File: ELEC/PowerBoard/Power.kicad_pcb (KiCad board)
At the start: 2 copper layers, 42.7 x 46.7 mm, 2 parts, among them J1 CONN_01X08, J2 CONN_01X08

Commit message: Added roadmap, worked on power board
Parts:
- added C1: 220uF, Capacitors_SMD:CP_Elec_8x10.5, F.Cu at (100.2, 94.5)
- added C2: 220uF, Capacitors_SMD:CP_Elec_8x10.5, F.Cu at (119.3, 94.6)
- added C3: 220uF, Capacitors_SMD:CP_Elec_8x10.5, F.Cu at (123.6, 82.7)
- added C4: 220uF, Capacitors_SMD:CP_Elec_8x10.5, F.Cu at (109.7, 94.6)
- added C5: 10uF, Capacitors_SMD:C_1206, F.Cu at (102.4, 85.3)
- added C6: 10uF, Capacitors_SMD:C_1206, F.Cu at (106.2, 85.3)
- added C7: 10uF, Capacitors_SMD:C_1206, F.Cu at (98.6, 85.3)
- added C8: 0.1uF, Capacitors_SMD:C_0805, F.Cu at (109.7, 85.3)
- added J3: Barrel_Jack, Connectors_Barrel.pretty:PJ-082BH, F.Cu at (94.7, 109.5)
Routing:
- net (no net): track 444.9 -> 1.27 mm, vias 6 -> 0
- removed copper zone on B.Cu, net +24V
- removed copper zone on F.Cu, net +24V
- removed copper zone on B.Cu, net GND
- removed copper zone on F.Cu, net GND
- removed copper zone on F.Cu, net Net-(C10-Pad1)
- removed copper zone on F.Cu, net Net-(C11-Pad2)
- removed copper zone on F.Cu, net Net-(C14-Pad2)
- removed copper zone on F.Cu, net Net-(C15-Pad1)
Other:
- board text removed: "GAIN0"
- board text removed: "GAIN1"
- board text removed: "Left"
- board text removed: "Out"
- board text removed: "Right"
- board text removed: "SLAVE"

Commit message: Worked on power distrobution PCB
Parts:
- added J4: XT60 Connector, Connectors_Battery:XT60_Inline, F.Cu at (132.7, 90.9)
- moved J3 44.7 mm to (139.3, 105.9), turned to 180 degrees
- moved C6 27.7 mm to (133.3, 80.1), turned to 0 degrees
- moved C5 26.8 mm to (129.0, 82.8), turned to 0 degrees
- moved C1 22.4 mm to (106.9, 115.8), turned to 0 degrees
- moved C7 20.0 mm to (118.2, 88.6), turned to 0 degrees
- moved C3 17.2 mm to (106.9, 86.9)
- moved C2 16.9 mm to (106.9, 106.2), turned to 0 degrees
- moved C8 8.00 mm to (117.7, 85.5), turned to 0 degrees
- moved C4 3.38 mm to (106.9, 96.5), turned to 0 degrees

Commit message: Did a whole whack on the power PCB
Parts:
- removed C5, C6, C7: 10uF, Capacitors_SMD:C_1206
- removed C8: 0.1uF, Capacitors_SMD:C_0805
- added J5: CONN_02X03, Pin_Headers:Pin_Header_Straight_2x03_Pitch1.27mm, F.Cu at (127.8, 83.4)
- added Q1: MOSFET_8PIN, Housings_SOIC.pretty:SOIC-8_3.9x4.9mm_Pitch1.27mm, F.Cu at (112.5, 86.0)
- added R1: 1M, Resistors_SMD:R_0805, F.Cu at (131.6, 82.2)
- added R2: 422K, Resistors_SMD:R_0805, F.Cu at (123.2, 79.4)
- added R3: 316K, Resistors_SMD:R_0805, F.Cu at (123.2, 81.3)
- added R4: 243K, Resistors_SMD:R_0805, F.Cu at (123.2, 83.2)
- added R5: 1M, Resistors_SMD:R_0805, F.Cu at (117.5, 86.4)
- added R6: 1M, Resistors_SMD:R_0805, F.Cu at (115.6, 95.2)
- added R7: 1M, Resistors_SMD:R_0805, F.Cu at (114.3, 91.4)
- added Rh1: 1.32M, Resistors_SMD:R_0805, F.Cu at (123.2, 85.7)
- added Rx1: 220K, Resistors_SMD:R_0805, F.Cu at (127.0, 90.2)
- added Ry1: 1M, Resistors_SMD:R_0805, F.Cu at (129.5, 90.2)
- added U1: LM9036MX, Housings_SOIC.pretty:SOIC-8_3.9x4.9mm_Pitch1.27mm, F.Cu at (121.3, 102.2)
- added U2: LMV358, Housings_SOIC.pretty:SOIC-8_3.9x4.9mm_Pitch1.27mm, F.Cu at (121.3, 91.4)
- moved C1 5.72 mm to (101.2, 115.8)
- moved C2 5.72 mm to (101.2, 106.2)
- moved C3 5.72 mm to (101.2, 86.9)
- moved C4 5.72 mm to (101.2, 96.5)
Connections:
- J1 pad 5: GND -> Net-(J1-Pad5)
- J1 pad 6: GND -> Net-(J1-Pad5)
- J1 pad 7: GND -> Net-(J1-Pad5)
- J1 pad 8: GND -> Net-(J1-Pad5)
- J2 pad 1: (no net) -> Net-(J2-Pad1)
- J2 pad 2: (no net) -> Net-(J2-Pad2)
- J2 pad 3: (no net) -> Net-(J2-Pad3)
- J2 pad 4: (no net) -> Net-(J2-Pad4)
- J2 pad 5: (no net) -> /AUX_L
- J2 pad 6: (no net) -> /AUX_R
- J2 pad 7: (no net) -> GNDA
- J2 pad 8: (no net) -> /SYNC
- J4 pad 1: (no net) -> +24V
- J4 pad 2: (no net) -> GND
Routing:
- net +24V: track 0.00 -> 10.8 mm
- net Vref: track 0.00 -> 5.40 mm
- net Net-(J5-Pad6): track 0.00 -> 2.80 mm
- net Net-(J5-Pad4): track 0.00 -> 2.72 mm
- net Net-(J5-Pad2): track 0.00 -> 2.71 mm
- net Net-(Q1-Pad4): track 0.00 -> 1.86 mm
- net (no net): track 1.27 -> 0.00 mm
- net /AUX_R: track 0.00 -> 0.72 mm
- net /SYNC: track 0.00 -> 0.55 mm
- added copper zone on B.Cu, net +24V
- added copper zone on F.Cu, net GND
- added copper zone on F.Cu, net Net-(J1-Pad5)

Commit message: Finished Power PCB
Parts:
- added C10: 1uF, Capacitors_SMD:C_0805, F.Cu at (121.9, 97.2)
- added C5: 100nF, Capacitors_SMD:C_0805, F.Cu at (121.3, 108.0)
- added C6: 10uF, Capacitors_SMD:C_0805, F.Cu at (123.2, 108.0)
- added C7: 100nF, Capacitors_SMD:C_0805, F.Cu at (120.0, 95.2)
- added C8: 10uF, Capacitors_SMD:C_0805, F.Cu at (116.2, 95.9)
- added C9: 100nF, Capacitors_SMD:C_0805, F.Cu at (125.7, 99.1)
- added REF**: Vias, Via:10mil_Via, F.Cu at (97.2, 83.2)
- added REF**: Vias, Via:10mil_Via, F.Cu at (99.1, 83.8)
- added REF**: Vias, Via:10mil_Via, F.Cu at (98.4, 118.1)
- added REF**: Vias, Via:10mil_Via, F.Cu at (100.3, 118.1)
- added REF**: Vias, Via:10mil_Via, F.Cu at (99.7, 118.1)
- added REF**: Vias, Via:10mil_Via, F.Cu at (99.7, 118.7)
- added REF**: Vias, Via:10mil_Via, F.Cu at (100.3, 118.7)
- added REF**: Vias, Via:10mil_Via, F.Cu at (98.4, 118.7)
- added REF**: Vias, Via:10mil_Via, F.Cu at (99.1, 118.7)
- added REF**: Vias, Via:10mil_Via, F.Cu at (97.8, 118.7)
- added REF**: Vias, Via:10mil_Via, F.Cu at (97.2, 118.7)
- added REF**: Vias, Via:10mil_Via, F.Cu at (97.2, 111.8)
- added REF**: Vias, Via:10mil_Via, F.Cu at (97.8, 83.8)
- added REF**: Vias, Via:10mil_Via, F.Cu at (97.8, 111.8)
- added REF**: Vias, Via:10mil_Via, F.Cu at (99.1, 111.8)
- added REF**: Vias, Via:10mil_Via, F.Cu at (98.4, 111.8)
- added REF**: Vias, Via:10mil_Via, F.Cu at (100.3, 111.8)
- added REF**: Vias, Via:10mil_Via, F.Cu at (99.7, 111.8)
- added REF**: Vias, Via:10mil_Via, F.Cu at (99.7, 112.4)
- added REF**: Vias, Via:10mil_Via, F.Cu at (100.3, 112.4)
- added REF**: Vias, Via:10mil_Via, F.Cu at (98.4, 112.4)
- added REF**: Vias, Via:10mil_Via, F.Cu at (99.1, 112.4)
- added REF**: Vias, Via:10mil_Via, F.Cu at (97.8, 112.4)
- added REF**: Vias, Via:10mil_Via, F.Cu at (97.2, 83.8)
- added REF**: Vias, Via:10mil_Via, F.Cu at (97.2, 112.4)
- added REF**: Vias, Via:10mil_Via, F.Cu at (97.2, 113.7)
- added REF**: Vias, Via:10mil_Via, F.Cu at (97.8, 113.7)
- added REF**: Vias, Via:10mil_Via, F.Cu at (99.1, 113.7)
- added REF**: Vias, Via:10mil_Via, F.Cu at (98.4, 113.7)
- added REF**: Vias, Via:10mil_Via, F.Cu at (100.3, 113.7)
- added REF**: Vias, Via:10mil_Via, F.Cu at (99.7, 113.7)
- added REF**: Vias, Via:10mil_Via, F.Cu at (99.7, 113.0)
- added REF**: Vias, Via:10mil_Via, F.Cu at (100.3, 113.0)
- added REF**: Vias, Via:10mil_Via, F.Cu at (98.4, 113.0)
- added REF**: Vias, Via:10mil_Via, F.Cu at (97.2, 85.1)
- added REF**: Vias, Via:10mil_Via, F.Cu at (99.1, 113.0)
- added REF**: Vias, Via:10mil_Via, F.Cu at (97.8, 113.0)
- added REF**: Vias, Via:10mil_Via, F.Cu at (97.2, 113.0)
- added REF**: Vias, Via:10mil_Via, F.Cu at (97.2, 108.6)
- added REF**: Vias, Via:10mil_Via, F.Cu at (97.8, 108.6)
- added REF**: Vias, Via:10mil_Via, F.Cu at (99.1, 108.6)
- added REF**: Vias, Via:10mil_Via, F.Cu at (98.4, 108.6)
- added REF**: Vias, Via:10mil_Via, F.Cu at (100.3, 108.6)
- added REF**: Vias, Via:10mil_Via, F.Cu at (99.7, 108.6)
- added REF**: Vias, Via:10mil_Via, F.Cu at (99.7, 109.2)
- added REF**: Vias, Via:10mil_Via, F.Cu at (97.8, 85.1)
- added REF**: Vias, Via:10mil_Via, F.Cu at (100.3, 109.2)
- added REF**: Vias, Via:10mil_Via, F.Cu at (98.4, 109.2)
- added REF**: Vias, Via:10mil_Via, F.Cu at (99.1, 109.2)
- added REF**: Vias, Via:10mil_Via, F.Cu at (97.8, 109.2)
- added REF**: Vias, Via:10mil_Via, F.Cu at (97.2, 109.2)
- added REF**: Vias, Via:10mil_Via, F.Cu at (97.2, 110.5)
- added REF**: Vias, Via:10mil_Via, F.Cu at (97.8, 110.5)
- added REF**: Vias, Via:10mil_Via, F.Cu at (99.1, 110.5)
- added REF**: Vias, Via:10mil_Via, F.Cu at (98.4, 110.5)
- added REF**: Vias, Via:10mil_Via, F.Cu at (100.3, 110.5)
- added REF**: Vias, Via:10mil_Via, F.Cu at (99.1, 85.1)
- added REF**: Vias, Via:10mil_Via, F.Cu at (99.7, 110.5)
- added REF**: Vias, Via:10mil_Via, F.Cu at (99.7, 109.9)
- added REF**: Vias, Via:10mil_Via, F.Cu at (100.3, 109.9)
- added REF**: Vias, Via:10mil_Via, F.Cu at (98.4, 109.9)
- added REF**: Vias, Via:10mil_Via, F.Cu at (99.1, 109.9)
- added REF**: Vias, Via:10mil_Via, F.Cu at (97.8, 109.9)
- added REF**: Vias, Via:10mil_Via, F.Cu at (97.2, 109.9)
- added REF**: Vias, Via:10mil_Via, F.Cu at (97.2, 102.2)
- added REF**: Vias, Via:10mil_Via, F.Cu at (97.8, 102.2)
- added REF**: Vias, Via:10mil_Via, F.Cu at (99.1, 102.2)
- added REF**: Vias, Via:10mil_Via, F.Cu at (98.4, 85.1)
- added REF**: Vias, Via:10mil_Via, F.Cu at (98.4, 102.2)
- added REF**: Vias, Via:10mil_Via, F.Cu at (100.3, 102.2)
- added REF**: Vias, Via:10mil_Via, F.Cu at (99.7, 102.2)
- added REF**: Vias, Via:10mil_Via, F.Cu at (99.7, 102.9)
- added REF**: Vias, Via:10mil_Via, F.Cu at (100.3, 102.9)
- added REF**: Vias, Via:10mil_Via, F.Cu at (98.4, 102.9)
- added REF**: Vias, Via:10mil_Via, F.Cu at (99.1, 102.9)
- added REF**: Vias, Via:10mil_Via, F.Cu at (97.8, 102.9)
- added REF**: Vias, Via:10mil_Via, F.Cu at (97.2, 102.9)
- added REF**: Vias, Via:10mil_Via, F.Cu at (97.2, 104.1)
- added REF**: Vias, Via:10mil_Via, F.Cu at (100.3, 85.1)
- added REF**: Vias, Via:10mil_Via, F.Cu at (97.8, 104.1)
- added REF**: Vias, Via:10mil_Via, F.Cu at (99.1, 104.1)
- added REF**: Vias, Via:10mil_Via, F.Cu at (98.4, 104.1)
- added REF**: Vias, Via:10mil_Via, F.Cu at (100.3, 104.1)
- added REF**: Vias, Via:10mil_Via, F.Cu at (99.7, 104.1)
- added REF**: Vias, Via:10mil_Via, F.Cu at (99.7, 103.5)
- added REF**: Vias, Via:10mil_Via, F.Cu at (100.3, 103.5)
- added REF**: Vias, Via:10mil_Via, F.Cu at (98.4, 103.5)
- added REF**: Vias, Via:10mil_Via, F.Cu at (99.1, 103.5)
- added REF**: Vias, Via:10mil_Via, F.Cu at (97.8, 103.5)
- added REF**: Vias, Via:10mil_Via, F.Cu at (99.7, 85.1)
- added REF**: Vias, Via:10mil_Via, F.Cu at (97.2, 103.5)
- added REF**: Vias, Via:10mil_Via, F.Cu at (99.7, 84.5)
- added REF**: Vias, Via:10mil_Via, F.Cu at (97.8, 83.2)
- added REF**: Vias, Via:10mil_Via, F.Cu at (100.3, 84.5)
- added REF**: Vias, Via:10mil_Via, F.Cu at (98.4, 84.5)
- added REF**: Vias, Via:10mil_Via, F.Cu at (99.1, 84.5)
- added REF**: Vias, Via:10mil_Via, F.Cu at (97.8, 84.5)
- added REF**: Vias, Via:10mil_Via, F.Cu at (97.2, 84.5)
- added REF**: Vias, Via:10mil_Via, F.Cu at (97.2, 88.9)
- added REF**: Vias, Via:10mil_Via, F.Cu at (97.8, 88.9)
- added REF**: Vias, Via:10mil_Via, F.Cu at (99.1, 88.9)
- added REF**: Vias, Via:10mil_Via, F.Cu at (98.4, 88.9)
- added REF**: Vias, Via:10mil_Via, F.Cu at (100.3, 88.9)
- added REF**: Vias, Via:10mil_Via, F.Cu at (99.1, 83.2)
- added REF**: Vias, Via:10mil_Via, F.Cu at (99.7, 88.9)
- added REF**: Vias, Via:10mil_Via, F.Cu at (99.7, 89.5)
- added REF**: Vias, Via:10mil_Via, F.Cu at (100.3, 89.5)
- added REF**: Vias, Via:10mil_Via, F.Cu at (98.4, 89.5)
- added REF**: Vias, Via:10mil_Via, F.Cu at (99.1, 89.5)
- added REF**: Vias, Via:10mil_Via, F.Cu at (97.8, 89.5)
- added REF**: Vias, Via:10mil_Via, F.Cu at (97.2, 89.5)
- added REF**: Vias, Via:10mil_Via, F.Cu at (97.2, 90.8)
- added REF**: Vias, Via:10mil_Via, F.Cu at (97.8, 90.8)
- added REF**: Vias, Via:10mil_Via, F.Cu at (99.1, 90.8)
- added REF**: Vias, Via:10mil_Via, F.Cu at (98.4, 83.2)
- added REF**: Vias, Via:10mil_Via, F.Cu at (98.4, 90.8)
- added REF**: Vias, Via:10mil_Via, F.Cu at (100.3, 90.8)
- added REF**: Vias, Via:10mil_Via, F.Cu at (99.7, 90.8)
- added REF**: Vias, Via:10mil_Via, F.Cu at (99.7, 90.2)
- added REF**: Vias, Via:10mil_Via, F.Cu at (100.3, 90.2)
- added REF**: Vias, Via:10mil_Via, F.Cu at (98.4, 90.2)
- added REF**: Vias, Via:10mil_Via, F.Cu at (99.1, 90.2)
- added REF**: Vias, Via:10mil_Via, F.Cu at (97.8, 90.2)
- added REF**: Vias, Via:10mil_Via, F.Cu at (97.2, 90.2)
- added REF**: Vias, Via:10mil_Via, F.Cu at (97.2, 92.7)
- added REF**: Vias, Via:10mil_Via, F.Cu at (100.3, 83.2)
- added REF**: Vias, Via:10mil_Via, F.Cu at (97.8, 92.7)
- added REF**: Vias, Via:10mil_Via, F.Cu at (99.1, 92.7)
- added REF**: Vias, Via:10mil_Via, F.Cu at (98.4, 92.7)
- added REF**: Vias, Via:10mil_Via, F.Cu at (100.3, 92.7)
- added REF**: Vias, Via:10mil_Via, F.Cu at (99.7, 92.7)
- added REF**: Vias, Via:10mil_Via, F.Cu at (99.7, 93.3)
- added REF**: Vias, Via:10mil_Via, F.Cu at (100.3, 93.3)
- added REF**: Vias, Via:10mil_Via, F.Cu at (98.4, 93.3)
- added REF**: Vias, Via:10mil_Via, F.Cu at (99.1, 93.3)
- added REF**: Vias, Via:10mil_Via, F.Cu at (97.8, 93.3)
- added REF**: Vias, Via:10mil_Via, F.Cu at (99.7, 83.2)
- added REF**: Vias, Via:10mil_Via, F.Cu at (97.2, 93.3)
- added REF**: Vias, Via:10mil_Via, F.Cu at (97.2, 94.6)
- added REF**: Vias, Via:10mil_Via, F.Cu at (97.8, 94.6)
- added REF**: Vias, Via:10mil_Via, F.Cu at (99.1, 94.6)
- added REF**: Vias, Via:10mil_Via, F.Cu at (98.4, 94.6)
- added REF**: Vias, Via:10mil_Via, F.Cu at (100.3, 94.6)
- added REF**: Vias, Via:10mil_Via, F.Cu at (99.7, 94.6)
- added REF**: Vias, Via:10mil_Via, F.Cu at (99.7, 94.0)
- added REF**: Vias, Via:10mil_Via, F.Cu at (100.3, 94.0)
- added REF**: Vias, Via:10mil_Via, F.Cu at (98.4, 94.0)
- added REF**: Vias, Via:10mil_Via, F.Cu at (99.7, 83.8)
- added REF**: Vias, Via:10mil_Via, F.Cu at (99.1, 94.0)
- added REF**: Vias, Via:10mil_Via, F.Cu at (97.8, 94.0)
- added REF**: Vias, Via:10mil_Via, F.Cu at (97.2, 94.0)
- added REF**: Vias, Via:10mil_Via, F.Cu at (97.2, 98.4)
- added REF**: Vias, Via:10mil_Via, F.Cu at (97.8, 98.4)
- added REF**: Vias, Via:10mil_Via, F.Cu at (99.1, 98.4)
- added REF**: Vias, Via:10mil_Via, F.Cu at (98.4, 98.4)
- added REF**: Vias, Via:10mil_Via, F.Cu at (100.3, 98.4)
- added REF**: Vias, Via:10mil_Via, F.Cu at (99.7, 98.4)
- added REF**: Vias, Via:10mil_Via, F.Cu at (99.7, 99.1)
- added REF**: Vias, Via:10mil_Via, F.Cu at (100.3, 83.8)
- added REF**: Vias, Via:10mil_Via, F.Cu at (100.3, 99.1)
- added REF**: Vias, Via:10mil_Via, F.Cu at (98.4, 99.1)
- added REF**: Vias, Via:10mil_Via, F.Cu at (99.1, 99.1)
- added REF**: Vias, Via:10mil_Via, F.Cu at (97.8, 99.1)
- added REF**: Vias, Via:10mil_Via, F.Cu at (97.2, 99.1)
- added REF**: Vias, Via:10mil_Via, F.Cu at (97.2, 100.3)
- added REF**: Vias, Via:10mil_Via, F.Cu at (97.8, 100.3)
- added REF**: Vias, Via:10mil_Via, F.Cu at (99.1, 100.3)
- added REF**: Vias, Via:10mil_Via, F.Cu at (98.4, 100.3)
- added REF**: Vias, Via:10mil_Via, F.Cu at (100.3, 100.3)
- added REF**: Vias, Via:10mil_Via, F.Cu at (98.4, 83.8)
- added REF**: Vias, Via:10mil_Via, F.Cu at (99.7, 100.3)
- added REF**: Vias, Via:10mil_Via, F.Cu at (99.7, 99.7)
- added REF**: Vias, Via:10mil_Via, F.Cu at (100.3, 99.7)
- added REF**: Vias, Via:10mil_Via, F.Cu at (98.4, 99.7)
- added REF**: Vias, Via:10mil_Via, F.Cu at (99.1, 99.7)
- added REF**: Vias, Via:10mil_Via, F.Cu at (97.8, 99.7)
- added REF**: Vias, Via:10mil_Via, F.Cu at (97.2, 99.7)
- added REF**: Vias, Via:10mil_Via, F.Cu at (97.2, 118.1)
- added REF**: Vias, Via:10mil_Via, F.Cu at (97.8, 118.1)
- added REF**: Vias, Via:10mil_Via, F.Cu at (99.1, 118.1)
- moved R1 5.24 mm to (129.5, 87.0), turned to 90 degrees
- moved Rh1 4.84 mm to (118.7, 87.6)
- moved R5 4.02 mm to (116.2, 90.2)
- moved Rx1 2.54 mm to (127.0, 92.7)
- moved Ry1 2.54 mm to (129.5, 92.7)
- moved R6 2.01 mm to (116.2, 93.3)
- moved R7 0.63 mm to (113.7, 91.4)
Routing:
- net +5V: track 0.00 -> 21.2 mm
- net Vref: track 5.40 -> 20.2 mm
- net Net-(Rh1-Pad2): track 0.00 -> 12.4 mm
- net Net-(R5-Pad2): track 0.00 -> 12.3 mm
- net Net-(Q1-Pad4): track 1.86 -> 11.8 mm
- net GND: track 0.00 -> 4.51 mm
- net Net-(R5-Pad1): track 0.00 -> 3.79 mm
- net +24V: track 10.8 -> 11.8 mm
- added copper zone on F.Cu, net +24V
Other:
- board text added: "4Cell 5Cell 6Cell"
- board text added: "SoundHive PowerPCB Machinehum"
- board text added: "V0.1"
- board text added: "WARNING: Never plug in battery at the same time as DC power!"

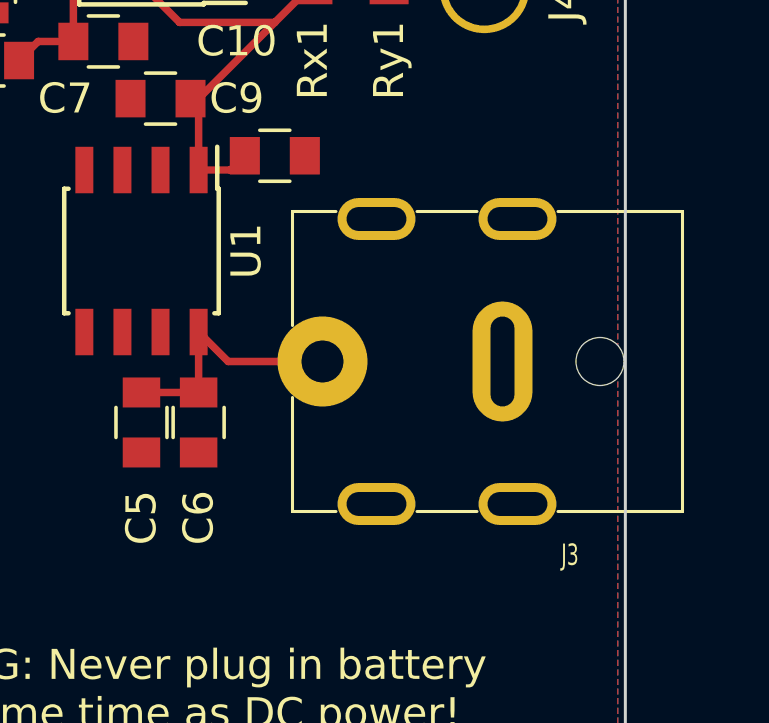
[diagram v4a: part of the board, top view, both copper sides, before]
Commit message: -Filled in P/N -Generated BOM -Ordered PCBs
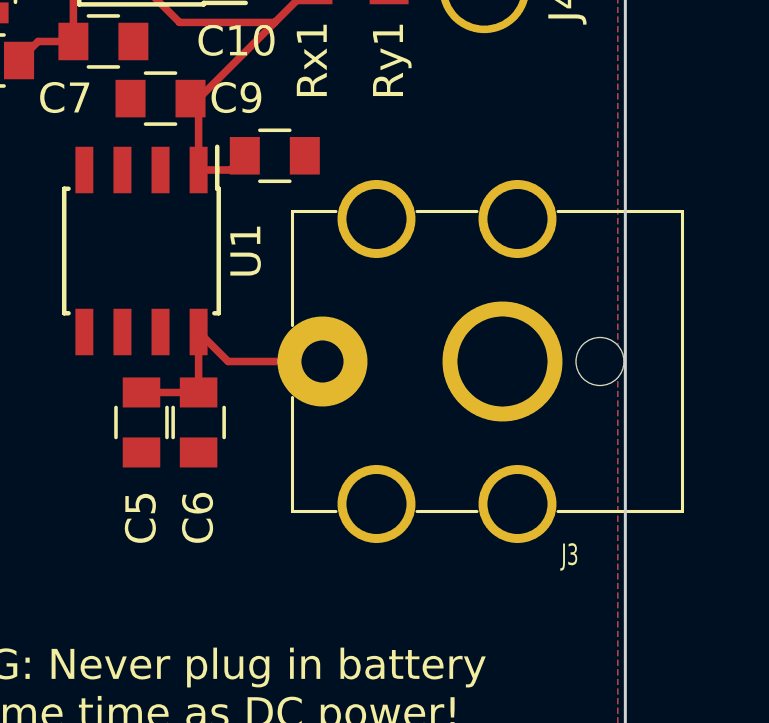
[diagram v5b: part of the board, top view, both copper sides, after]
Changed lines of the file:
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@@
-(kicad_pcb (version 4) (host pcbnew 4.0.5+dfsg1-4)
+(kicad_pcb (version 4) (host pcbnew 4.0.5+dfsg1-4~bpo8+1)
   (general
     (links 252)
@@
     (mod_text_size 1 1)
     (mod_text_width 0.15)
-    (pad_size 0.381 0.381)
-    (pad_drill 0.254)
+    (pad_size 2.6 2.6)
+    (pad_drill 2)
     (pad_to_mask_clearance 0)
     (aux_axis_origin 94.742 124.714)
@@
     (pad 1 thru_hole circle (at 12 0 180) (size 3 3) (drill 1.4) (layers *.Cu *.Mask)
       (net 2 +24V))
-    (pad 2 thru_hole oval (at 5.5 -4.75 180) (size 2.6 1.4) (drill oval 2 0.8) (layers *.Cu *.Mask)
+    (pad 2 thru_hole oval (at 5.5 -4.75 180) (size 2.6 2.6) (drill oval 2) (layers *.Cu *.Mask)
       (net 1 GND))
-    (pad 2 thru_hole oval (at 10.2 -4.75 180) (size 2.6 1.4) (drill oval 2 0.8) (layers *.Cu *.Mask)
+    (pad 2 thru_hole oval (at 10.2 -4.75 180) (size 2.6 2.6) (drill oval 2) (layers *.Cu *.Mask)
       (net 1 GND))
-    (pad 2 thru_hole oval (at 5.5 4.75 180) (size 2.6 1.4) (drill oval 2 0.8) (layers *.Cu *.Mask)
+    (pad 2 thru_hole oval (at 5.5 4.75 180) (size 2.6 2.6) (drill oval 2) (layers *.Cu *.Mask)
       (net 1 GND))
-    (pad 2 thru_hole oval (at 10.2 4.75 180) (size 2.6 1.4) (drill oval 2 0.8) (layers *.Cu *.Mask)
+    (pad 2 thru_hole oval (at 10.2 4.75 180) (size 2.6 2.6) (drill oval 2) (layers *.Cu *.Mask)
       (net 1 GND))
-    (pad 2 thru_hole oval (at 6 0 270) (size 4 2) (drill oval 3 0.8) (layers *.Cu *.Mask)
+    (pad 2 thru_hole oval (at 6 0 270) (size 4 4) (drill oval 3) (layers *.Cu *.Mask)
       (net 1 GND))
     (model ${KIPRJMOD}/../Libraries/3d_models/pj-082bh.wrl
